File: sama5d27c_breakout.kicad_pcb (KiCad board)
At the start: 4 copper layers, 70 x 74.5 mm, 231 parts, among them J1 Conn_LCD, J10 Conn_Speaker, J2 Conn_JTAG, J3 Conn_SDMMC0, J4 Conn_FLEXCOM3_4, J5 Conn_DBGU, J6 Conn_BAT, J7 USB_C_Receptacle_USB2.0, J8 USB_B_Micro, J9 Micro_SD_Card_Det, Q1 BSS138, Q2 BSS138, Q3 BSS138, Q4 BSS138, Q5 BSS138, SW1 SW_WAKEUP, SW2 SW_RESET, SW3 SW_USR, U1 SAMA5D2x-SIP, U2 ACT8945A, U3 MIC2025, U4 IS25LP128F, U5 DMC2450, U6 DMC2450, Y1 TSX-3225 24MHz, Y2 32kHz

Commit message: Almost routed, just 2 unconnected left
Hahahahahah HahahaHhahaHAHAhahahHAHAHAHhahah
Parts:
- removed TP10: TP_VDDBU, TestPoint:TestPoint_Pad_D1.5mm
- removed TP5: TP_3.3V, TestPoint:TestPoint_Pad_D1.5mm
- J1: footprint Connector_PinHeader_1.27mm:PinHeader_2x21_P1.27mm_Vertical -> Connector_PinHeader_1.27mm:PinHeader_2x19_P1.27mm_Vertical_SMD
- TP1, TP11, TP2, TP3, TP4, TP6, TP7, TP8, TP9: moved to B.Cu
- moved TP11 68.5 mm to (186.9, 61.0)
- moved TP8 55.0 mm to (128.2, 78.2)
- moved TP3 50.4 mm to (175.3, 82.0)
- moved TP2 46.6 mm to (129.3, 83.6)
- moved J5 46.2 mm to (132.8, 65.5)
- moved TP6 45.5 mm to (172.6, 84.0)
- moved TP7 45.0 mm to (137.0, 78.2)
- moved TP9 44.7 mm to (130.9, 76.9)
- moved TP1 42.3 mm to (136.3, 93.0)
- moved TP4 33.0 mm to (142.7, 88.4)
- moved J1 16.4 mm to (156.8, 52.3)
- moved J4 13.0 mm to (121.1, 50.0), turned to 0 degrees
- moved J2 11.1 mm to (130.8, 110.2)
- moved FB11 4.55 mm to (156.7, 105.6)
- moved FB10 4.55 mm to (173.6, 107.6)
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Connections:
- net Net-(FB10-Pad1) renamed /USB/B_GND
- net Net-(FB11-Pad1) renamed /USB/A_GND
- J1 pad 10: /SPI0_NPCS0 -> /LCD_DEN
- J1 pad 11: /SPI0_MISO -> /LCD_HSYNC
- J1 pad 12: /SPI0_MOSI -> /LCD_VSYNC
- J1 pad 13: /SPI0_SPCK -> /LCD_PCK
- J1 pad 14: /LCD_DEN -> /LCD_DAT0
- J1 pad 15: /LCD_HSYNC -> /LCD_DAT1
- J1 pad 16: /LCD_VSYNC -> /LCD_DAT2
- J1 pad 17: /LCD_PCK -> /LCD_DAT3
- J1 pad 18: /LCD_DAT0 -> /LCD_DAT4
- J1 pad 19: /LCD_DAT1 -> /LCD_DAT5
- J1 pad 20: /LCD_DAT2 -> /LCD_DAT6
- J1 pad 21: /LCD_DAT3 -> /LCD_DAT7
- J1 pad 22: /LCD_DAT4 -> /LCD_DAT8
- J1 pad 23: /LCD_DAT5 -> /LCD_DAT9
- J1 pad 24: /LCD_DAT6 -> /LCD_DAT10
- J1 pad 25: /LCD_DAT7 -> /LCD_DAT11
- J1 pad 26: /LCD_DAT8 -> /LCD_DAT12
- J1 pad 27: /LCD_DAT9 -> /LCD_DAT13
- J1 pad 28: /LCD_DAT10 -> /LCD_DAT14
- J1 pad 29: /LCD_DAT11 -> /LCD_DAT15
- J1 pad 30: /LCD_DAT12 -> /LCD_DAT16
- J1 pad 31: /LCD_DAT13 -> /LCD_DAT17
- J1 pad 32: /LCD_DAT14 -> /LCD_DAT18
- J1 pad 33: /LCD_DAT15 -> /LCD_DAT19
- J1 pad 34: /LCD_DAT16 -> /LCD_DAT20
- J1 pad 35: /LCD_DAT17 -> /LCD_DAT21
- J1 pad 36: /LCD_DAT18 -> /LCD_DAT22
- J1 pad 37: /LCD_DAT19 -> /LCD_DAT23
- J1 pad 38: /LCD_DAT20 -> Net-(J1-Pad38)
- U1 pad B10: Net-(U1-PadB10) -> /IRQ2
- U1 pad B2: /PMIC_LBO -> Net-(U1-PadB2)
- U1 pad F5: /LED_GREEN -> Net-(U1-PadF5)
- U1 pad F7: Net-(U1-PadF7) -> /LED_BLUE
- U1 pad G6: Net-(U1-PadG6) -> /LED_GREEN
- U1 pad H8: /IRQ2 -> /LED_RED
- U1 pad J2: Net-(U1-PadJ2) -> /PMIC_LBO
- U1 pad K8: Net-(U1-PadK8) -> /USBB_PWR_EN
- U1 pad L1: Net-(U1-PadL1) -> /PMIC_CHGLEV
- U1 pad M11: /SPI0_MISO -> Net-(U1-PadM11)
- U1 pad M17: /SPI0_SPCK -> Net-(U1-PadM17)
- U1 pad N1: Net-(U1-PadN1) -> /USR_BTN
- U1 pad N14: /SPI0_NPCS0 -> Net-(U1-PadN14)
- U1 pad N16: /SPI0_MOSI -> Net-(U1-PadN16)
- U1 pad N17: /PMIC_CHGLEV -> Net-(U1-PadN17)
- U1 pad P13: /LED_BLUE -> Net-(U1-PadP13)
- U1 pad P14: /USR_BTN -> Net-(U1-PadP14)
- U1 pad R10: /LED_RED -> Net-(U1-PadR10)
- U1 pad R15: /USBB_PWR_EN -> Net-(U1-PadR15)
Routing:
- net /nRST: track 1.38 -> 78.9 mm, vias 0 -> 5
- net /FLEXCOM3_IO2: track 0.57 -> 56.9 mm, vias 1 -> 3
- net +3V3: track 69.5 -> 117.7 mm, vias 10 -> 20
- net /FLEXCOM3_IO0: track 3.80 -> 49.6 mm, vias 1 -> 3
- net /JTAG_TCK: track 0.57 -> 45.2 mm, vias 1 -> 2
- net /LCD_TWCK: track 1.22 -> 45.8 mm, vias 1 -> 4
- net /JTAG_TDI: track 0.57 -> 43.6 mm, vias 1 -> 2
- net /JTAG_TMS: track 0.57 -> 43.4 mm, vias 1 -> 3
- net /JTAG_TDO: track 0.57 -> 43.2 mm, vias 1 -> 2
- net /FLEXCOM4_IO3: track 0.57 -> 43.0 mm, vias 1 -> 4
- net /FLEXCOM4_IO0: track 5.38 -> 46.9 mm, vias 1 -> 3
- net /FLEXCOM3_IO4: track 1.27 -> 42.6 mm, vias 1 -> 4
- net /FLEXCOM4_IO1: track 2.77 -> 44.1 mm, vias 1 -> 4
- net /FLEXCOM4_IO2: track 5.43 -> 46.5 mm, vias 1 -> 3
- net /LCD_TWD: track 0.57 -> 40.6 mm, vias 1 -> 4
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- added copper zone on F.Cu, net /USB/A_GND
- added copper zone on F.Cu, net /USB/B_GND
- added copper zone on B.Cu, net GND
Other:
- board size 70 x 74.5 mm -> 70 x 64 mm
- board text added: "3V"
- board text added: "CD"
- board text added: "CLK"
- board text added: "CMD"
- board text added: "D0"
- board text added: "D1"
- board text added: "D2"
- board text added: "D3"
- board text added: "D4"
- board text added: "D5"
- board text added: "D6"
- board text added: "D7"
- board text added: "GND"
- board text added: "VSE"

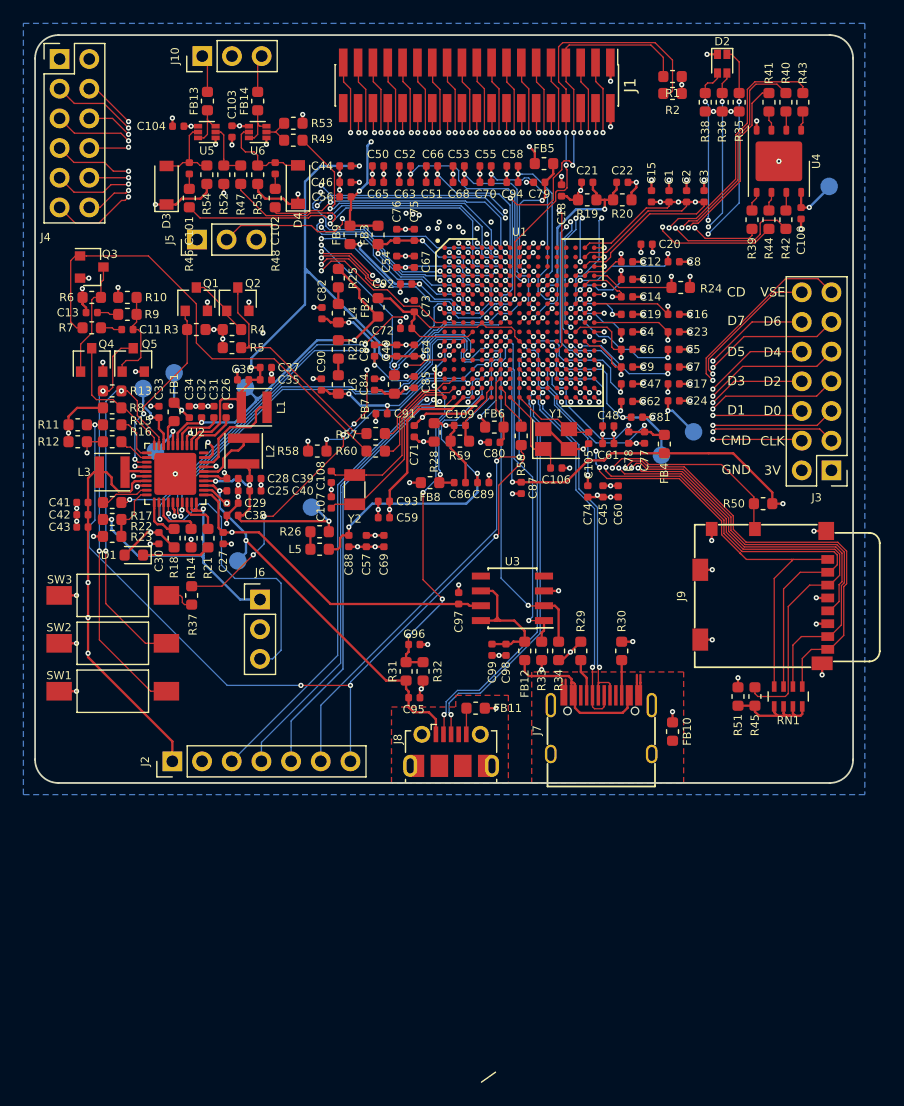
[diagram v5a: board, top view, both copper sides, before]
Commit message: Finish the routing, add bom, schematic
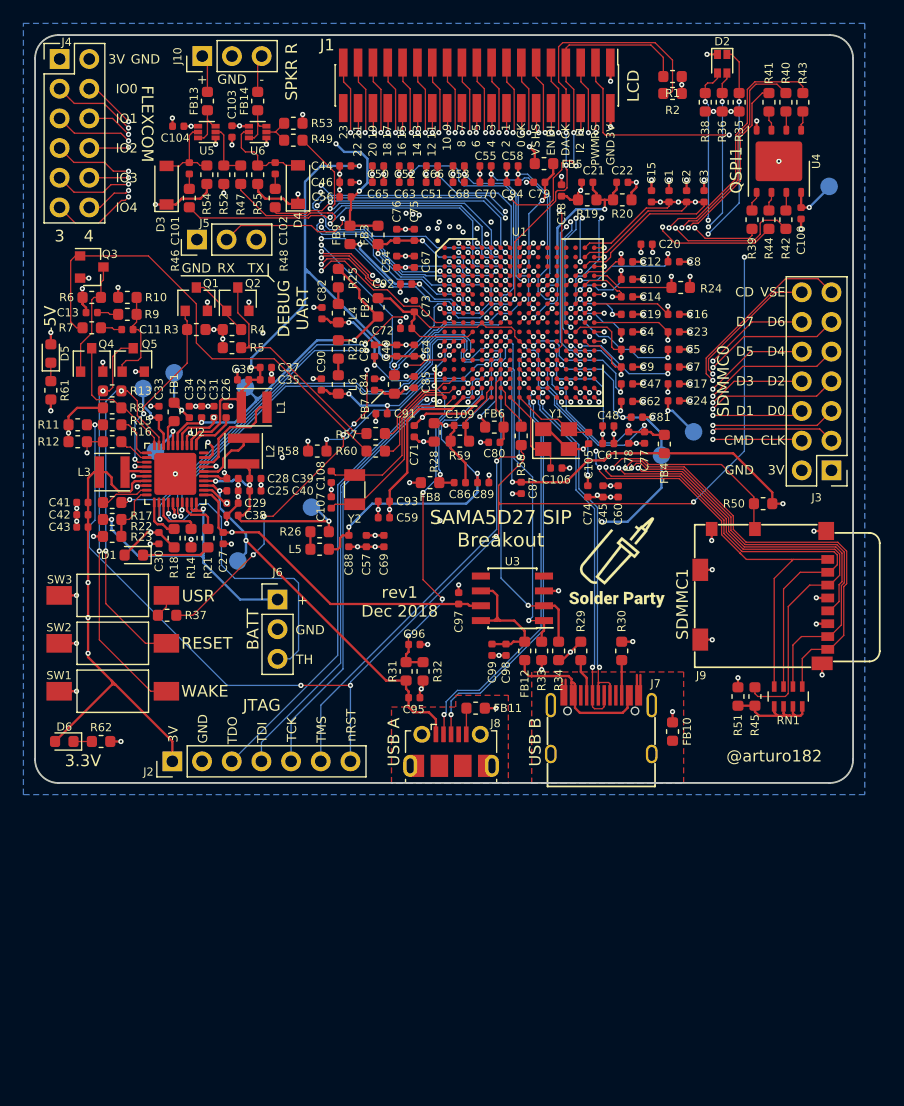
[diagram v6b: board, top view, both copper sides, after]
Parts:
- added D5: LED_5V, LED_SMD:LED_0603_1608Metric, F.Cu at (120.3, 75.2)
- added D6: LED_3V, LED_SMD:LED_0603_1608Metric, F.Cu at (121.5, 108.5)
- added G***: LOGO, Symbols_Extra:SolderParty-Logo_9.5x8.8mm_SilkScreen, F.Cu at (168.8, 93.1)
- added G***: LOGO, Symbols_Extra:SolderParty-Logo_14.6x13.5mm_SilkScreen, B.Cu at (180.3, 97.6)
- added R61: 2K, Resistor_SMD:R_0603_1608Metric, F.Cu at (120.3, 78.4)
- added R62: 1K, Resistor_SMD:R_0603_1608Metric, F.Cu at (124.7, 108.5)
- moved R37 2.70 mm to (130.3, 97.7), turned to 180 degrees
- moved J6 1.50 mm to (139.8, 96.3)
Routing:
- net /nRST: track 78.9 -> 140.6 mm, vias 5 -> 7
- net VDDFUSE: track 20.2 -> 66.2 mm, vias 2 -> 6
- net +3V3: track 117.7 -> 127.0 mm
- net /USR_BTN: track 33.7 -> 36.1 mm
- net GND: track 145.8 -> 147.7 mm, vias 158 -> 160
- net Net-(D6-Pad1): track 0.00 -> 1.58 mm
- net Net-(D5-Pad1): track 0.00 -> 1.58 mm
- net +BATT: track 24.2 -> 25.7 mm
- net /Power/BATT_TH: track 24.7 -> 26.2 mm
- net Net-(C79-Pad1): track 12.1 -> 10.8 mm
- net +5V: track 71.8 -> 72.8 mm, vias 16 -> 17
- net Net-(C77-Pad1): track 29.5 -> 30.5 mm
- net Net-(R37-Pad2): track 2.74 -> 2.00 mm
- net +1V35: track 275.1 -> 274.5 mm
- net Net-(U1-PadP14): track 0.57 -> 0.00 mm, vias 1 -> 0
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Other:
- rule pad_to_mask_clearance: 0.051 -> 0.05
- board text added: "+"
- board text added: "-"
- board text added: "-5V"
- board text added: "0"
- board text added: "1"
- board text added: "1.2V"
- board text added: "1.35V"
- board text added: "10"
- board text added: "11"
- board text added: "12"
- board text added: "13"
- board text added: "14"
- board text added: "15"
- board text added: "16"
- board text added: "17"
- board text added: "18"
- board text added: "19"
- board text added: "2"
- board text added: "20"
- board text added: "21"
- board text added: "22"
- board text added: "23"
- board text added: "3"
- board text added: "3.3V"
- board text added: "3.3VP"
- board text added: "4"
- board text added: "5"
- board text added: "5V"
- board text added: "6"
- board text added: "7"
- board text added: "8"
- board text added: "9"
- board text added: "@arturo182"
- board text added: "BATT"
- board text added: "CK"
- board text added: "DA"
- board text added: "DEBUG UART"
- board text added: "DI"
- board text added: "EN"
- board text added: "FLEXCOM"
- board text added: "HS"
- board text added: "I1"
- board text added: "I2"
- board text added: "IO0"
- board text added: "IO1"
- board text added: "IO2"
- board text added: "IO3"
- board text added: "IO4"
- board text added: "JTAG"
- board text added: "LCD"
- board text added: "PWM"
- board text added: "QSPI1"
- board text added: "RESET"
- board text added: "RS"
- board text added: "RX"
- board text added: "SAMA5D27 SIP Breakout"
- board text added: "SDMMC0"
- board text added: "SDMMC1"
- board text added: "SPKR R"
- board text added: "TCK"
- board text added: "TDI"
- board text added: "TDO"
- board text added: "TH"
- board text added: "TMS"
- board text added: "TX"
- board text added: "USB A"
- board text added: "USB B"
- board text added: "USR"
- board text added: "VBUS"
- board text added: "VDD LED"
- board text added: "VDDFUSE"
- board text added: "VDDSDHC"
- board text added: "VS"
- board text added: "WAKE"
- board text added: "nRST"
- board text added: "rev1 Dec 2018"
